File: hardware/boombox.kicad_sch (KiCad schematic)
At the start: 36 parts, among them J1 Micro_SD_Card_Det1, J4 USB_C_Receptacle_USB2.0_16P, SW1 SW_SPST, SW2 SW_SPST, SW3 SW_SPST, SW4 SW_SPST, SW5 SW_SPST, U1 Pico, U2 TMAG5231, U3 TMAG5231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

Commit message: Comitting so Nate can see errors
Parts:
- C11: value C_Small -> 0.1uF
- C3, C4: value C_Small -> 6pF
- J4: footprint (none) -> boombox:CUI_UJ20-C-H-C-4-SMT-TR
- U1: footprint RPi_Pico:RPi_Pico_SMD_TH -> boombox:RPi_Pico_SMD_TH
- U2, U3, U4, U5, U6: footprint (none) -> Package_TO_SOT_SMD:SOT-23
- Y1: footprint (none) -> boombox:XTAL_ECS-.327-6-13X
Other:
- title: (none) -> Boombuddy

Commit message: Routing
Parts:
- SW1: footprint boombox:PTS645S_SMTR92_CNK -> TestPoint:TestPoint_Pad_2.0x2.0mm
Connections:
- net BUTTONS0: now also SW1.1 (A); no longer SW1.2 (B)
- net BUTTONS1: now also SW2.1 (A); no longer SW2.2 (B)
- net BUTTONS2: now also SW3.1 (A); no longer SW3.2 (B)
- net BUTTONS3: now also SW4.1 (A); no longer SW4.2 (B)
- net BUTTONS4: now also SW5.1 (A); no longer SW5.2 (B)
- net SLP_PWR: now also SW1.2 (B), SW2.2 (B), SW3.2 (B), SW4.2 (B), SW5.2 (B); no longer SW1.1 (A), SW2.1 (A), SW3.1 (A), SW4.1 (A), SW5.1 (A)
- net USB_DN: now reaches J4.A7 (D-), J4.B7 (D-)
- net USB_DN: now also U1.45 (DP); no longer U1.44 (DN)
- net USB_DP: now reaches J4.A6 (D+), J4.B6 (D+)
- net USB_DP: now also U1.44 (DN); no longer U1.45 (DP)
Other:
- moved on the sheet: SW1, SW2, SW3, SW4, SW5
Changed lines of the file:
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@@
 	(wire
 		(pts
+			(xy 128.27 119.38) (xy 128.27 146.05)
+		)
+		(stroke
+			(width 0)
+			(type default)
+		)
+	)
+	(wire
+		(pts
 			(xy 92.71 158.75) (xy 92.71 146.05)
 		)
@@
 	(wire
 		(pts
+			(xy 107.95 111.76) (xy 107.95 146.05)
+		)
+		(stroke
+			(width 0)
+			(type default)
+		)
+	)
+	(wire
+		(pts
 			(xy 251.46 62.23) (xy 135.89 62.23)
 		)
@@
 	(wire
 		(pts
-			(xy 205.74 81.28) (xy 213.36 81.28)
+			(xy 97.79 109.22) (xy 97.79 146.05)
 		)
 		(stroke
@@
 	(wire
 		(pts
-			(xy 97.79 109.22) (xy 97.79 146.05)
+			(xy 205.74 81.28) (xy 213.36 81.28)
 		)
 		(stroke
@@
 	(wire
 		(pts
+			(xy 118.11 116.84) (xy 118.11 146.05)
+		)
+		(stroke
+			(width 0)
+			(type default)
+		)
+	)
+	(wire
+		(pts
 			(xy 77.47 96.52) (xy 138.43 96.52)
 		)
@@
 	(wire
 		(pts
-			(xy 118.11 146.05) (xy 118.11 116.84)
-		)
-		(stroke
-			(width 0)
-			(type default)
-		)
-	)
-	(wire
-		(pts
 			(xy 68.58 35.56) (xy 82.55 35.56)
 		)
@@
 	(wire
 		(pts
-			(xy 128.27 146.05) (xy 128.27 119.38)
-		)
-		(stroke
-			(width 0)
-			(type default)
-		)
-	)
-	(wire
-		(pts
 			(xy 48.26 72.39) (xy 93.98 72.39)
 		)
@@
 		)
 	)
-	(wire
-		(pts
-			(xy 107.95 146.05) (xy 107.95 111.76)
-		)
-		(stroke
-			(width 0)
-			(type default)
-		)
-	)
 	(bus
 		(pts
@@
 		)
 	)
+	(label "USB_DN"
+		(at 132.08 57.15 0)
+		(fields_autoplaced yes)
+		(effects
+			(font
+				(size 1.27 1.27)
+			)
+			(justify left bottom)
+		)
+	)
 	(label "BUTTONS2"
 		(at 102.87 158.75 90)
@@
 		)
 	)
+	(label "USB_DP"
+		(at 134.62 53.34 0)
+		(fields_autoplaced yes)
+		(effects
+			(font
+				(size 1.27 1.27)
+			)
+			(justify left bottom)
+		)
+	)
 	(symbol
 		(lib_id "Device:C_Small")
@@
 	(symbol
 		(lib_id "Switch:SW_SPST")
-		(at 92.71 138.43 270)
+		(at 92.71 138.43 90)
 		(unit 1)
 		(exclude_from_sim no)
@@
 		(dnp no)
 		(property "Reference" "SW2"
-			(at 89.916 136.398 0)
+			(at 95.504 140.462 0)
 			(effects
 				(font
@@
 		)
 		(property "Value" "SW_SPST"
-			(at 95.25 139.6999 90)
+			(at 90.17 137.1601 90)
 			(effects
 				(font
@@
 	(symbol
 		(lib_id "Switch:SW_SPST")
-		(at 123.19 138.43 270)
+		(at 123.19 138.43 90)
 		(unit 1)
 		(exclude_from_sim no)
@@
 		(dnp no)
 		(property "Reference" "SW5"
-			(at 120.904 136.398 0)
+			(at 125.476 140.462 0)
 			(effects
 				(font
@@
 		)
 		(property "Value" "SW_SPST"
-			(at 125.73 139.6999 90)
+			(at 120.65 137.1601 90)
 			(effects
 				(font
@@
 	(symbol
 		(lib_id "Switch:SW_SPST")
-		(at 113.03 138.43 270)
+		(at 113.03 138.43 90)
 		(unit 1)
 		(exclude_from_sim no)
@@
 		(dnp no)
 		(property "Reference" "SW4"
-			(at 110.744 136.398 0)
+			(at 115.316 140.462 0)
 			(effects
 				(font
@@
 		)
 		(property "Value" "SW_SPST"
-			(at 115.57 139.6999 90)
+			(at 110.49 137.1601 90)
 			(effects
 				(font
@@
 	(symbol
 		(lib_id "Switch:SW_SPST")
-		(at 102.87 138.43 270)
+		(at 102.87 138.43 90)
 		(unit 1)
 		(exclude_from_sim no)
@@
 		(dnp no)
 		(property "Reference" "SW3"
-			(at 100.33 136.398 0)
+			(at 105.41 140.462 0)
 			(effects
 				(font
@@
 		)
 		(property "Value" "SW_SPST"
-			(at 105.41 139.6999 90)
+			(at 100.33 137.1601 90)
 			(effects
 				(font
@@
 	(symbol
 		(lib_id "Switch:SW_SPST")
-		(at 81.28 138.43 270)
+		(at 81.28 138.43 90)
 		(unit 1)
 		(exclude_from_sim no)
@@
 		(dnp no)
 		(property "Reference" "SW1"
-			(at 77.978 135.89 0)
+			(at 84.582 140.97 0)
 			(effects
 				(font
@@
 		)
 		(property "Value" "SW_SPST"
-			(at 83.82 139.6999 90)
+			(at 78.74 137.1601 90)
 			(effects
 				(font
@@
 			)
 		)
-		(property "Footprint" "boombox:PTS645S_SMTR92_CNK"
+		(property "Footprint" "TestPoint:TestPoint_Pad_2.0x2.0mm"
 			(at 81.28 138.43 0)
 			(effects

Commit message: Switches
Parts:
- added TP1, TP10, TP2, TP3, TP4, TP5, TP6, TP7, TP8, TP9: ~, boombox:TestPoint_Pad_2.0x2.0mm, symbol Connector:TestPoint_Small
- added TP11, TP12: TestPoint_Small, boombox:TestPoint_Pad_2.0x2.0mm, symbol Connector:TestPoint_Small
- SW1: footprint TestPoint:TestPoint_Pad_2.0x2.0mm -> boombox:PTS645S_SMTR92_CNK
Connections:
- net BUTTONS0: now also TP2.1; no longer C5.1, SW1.1 (A), U1.15 (GPIO11)
- net BUTTONS1: now also TP4.1; no longer C6.1, SW2.1 (A), U1.16 (GPIO12)
- net BUTTONS2: now also TP6.1; no longer C7.1, SW3.1 (A), U1.17 (GPIO13)
- net BUTTONS3: now also TP8.1; no longer C8.1, SW4.1 (A), U1.19 (GPIO14)
- net BUTTONS4: now also TP10.1; no longer C9.1, SW5.1 (A), U1.20 (GPIO15)
- net SLP_PWR: now also TP11.1; no longer SW1.2 (B), SW2.2 (B), SW3.2 (B), SW4.2 (B), SW5.2 (B)
- new net: C8.1, SW4.1 (A), TP7.1, U1.19 (GPIO14)
- new net: C5.1, SW1.1 (A), TP1.1, U1.15 (GPIO11)
- new net: C7.1, SW3.1 (A), TP5.1, U1.17 (GPIO13)
- new net: C6.1, SW2.1 (A), TP3.1, U1.16 (GPIO12)
- new net: C9.1, SW5.1 (A), TP9.1, U1.20 (GPIO15)
- new net BTN_PWR: SW1.2 (B), SW2.2 (B), SW3.2 (B), SW4.2 (B), SW5.2 (B), TP12.1
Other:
- moved on the sheet: C5, C6, C7, C8, C9

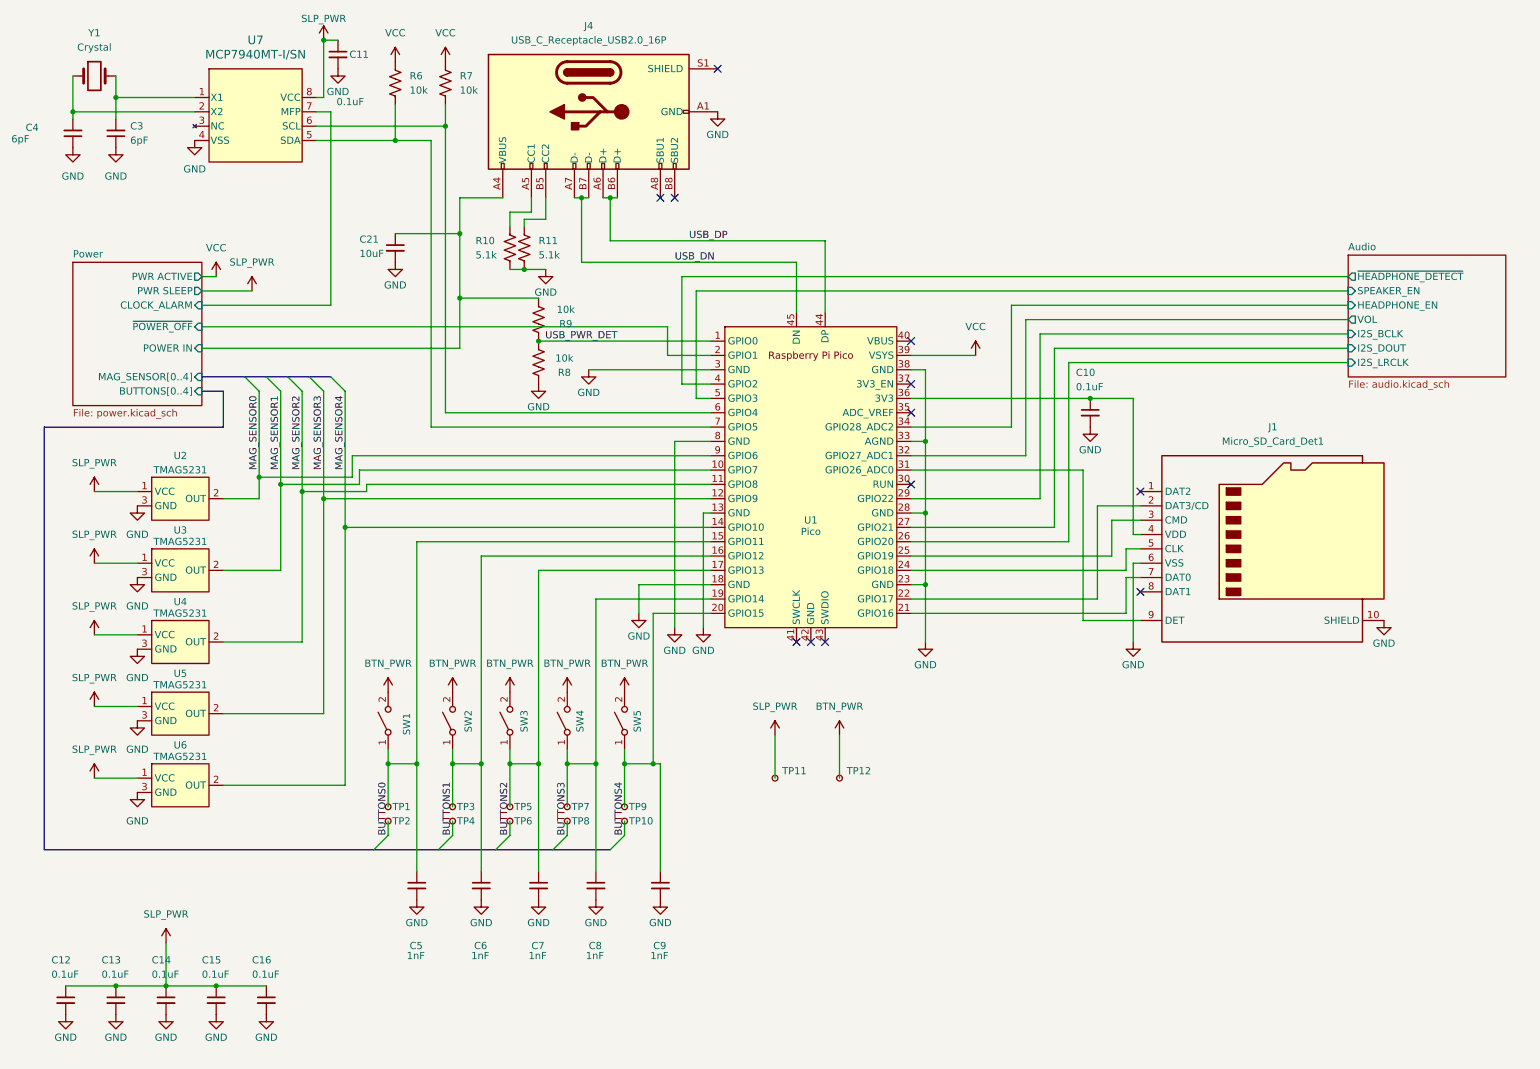
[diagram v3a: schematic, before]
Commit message: Resized cartridge and moved around things
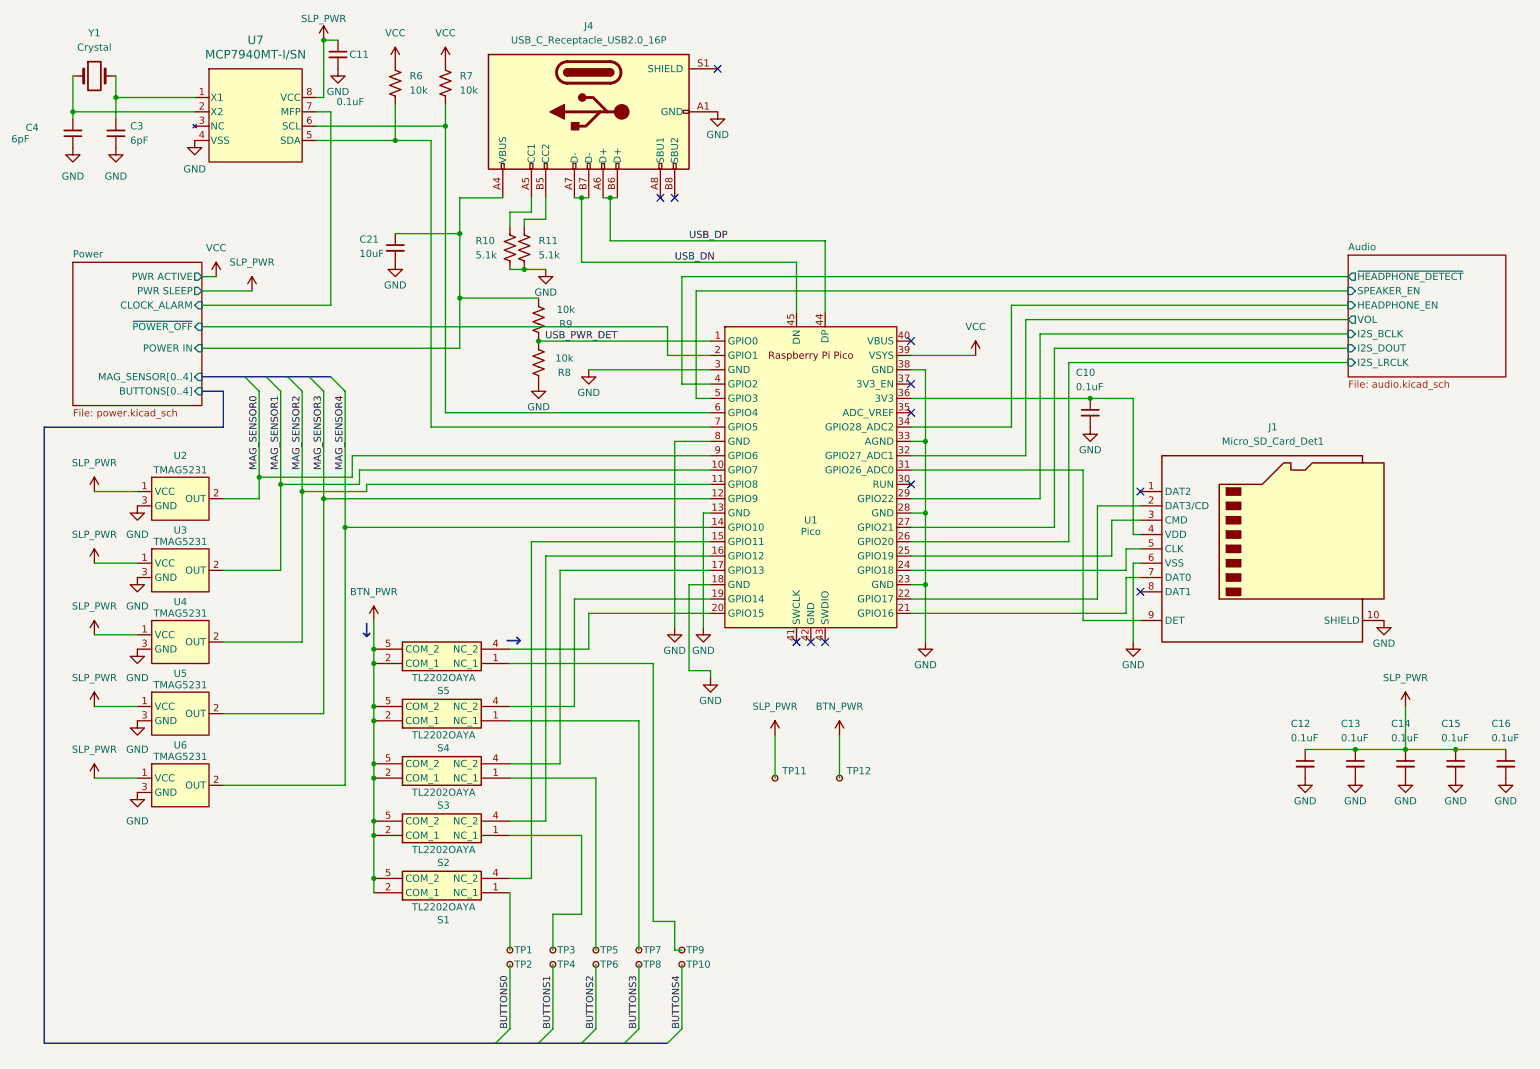
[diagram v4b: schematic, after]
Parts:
- removed C5, C6, C7, C8, C9: 1nF, Capacitor_SMD:C_0402_1005Metric_Pad0.74x0.62mm_HandSolder, symbol Device:C_Small
- removed SW1, SW2, SW3, SW4, SW5: SW_SPST, boombox:PTS645S_SMTR92_CNK, symbol Switch:SW_SPST
- added S1, S2, S3, S4, S5: TL2202OAYA, TL2202OAYA, symbol boombox:TL2202OAYA
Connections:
- net BTN_PWR: now also S1.2 (COM_1), S1.5 (COM_2), S2.2 (COM_1), S2.5 (COM_2), S3.2 (COM_1), S3.5 (COM_2), S4.2 (COM_1), S4.5 (COM_2), S5.2 (COM_1), S5.5 (COM_2)
- net at TP7.1: now also S4.1 (NC_1); no longer U1.19 (GPIO14)
- net at TP1.1: now also S1.1 (NC_1); no longer U1.15 (GPIO11)
- net at U1.17 (GPIO13): now also S3.4 (NC_2); no longer TP5.1
- net at TP3.1: now also S2.1 (NC_1); no longer U1.16 (GPIO12)
- net at U1.20 (GPIO15): now also S5.4 (NC_2); no longer TP9.1
- new net: S1.4 (NC_2), U1.15 (GPIO11)
- new net: S2.4 (NC_2), U1.16 (GPIO12)
- new net: S4.4 (NC_2), U1.19 (GPIO14)
- new net: S5.1 (NC_1), TP9.1
- new net: S3.1 (NC_1), TP5.1
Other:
- note added: "↓"
- moved on the sheet: C12, C13, C14, C15, C16, TP1, TP10, TP2, TP3, TP4, TP5, TP6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

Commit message: Almost done TM
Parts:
- removed TP10, TP6, TP7, TP9: ~, boombox:TestPoint_Pad_2.0x2.0mm, symbol Connector:TestPoint_Small
- removed TP11: TestPoint_Small, boombox:TestPoint_Pad_2.0x2.0mm, symbol Connector:TestPoint_Small
- added J2: Screw_Terminal_01x07, boombox:1990054, symbol Connector:Screw_Terminal_01x07
- TP1, TP2, TP3, TP4, TP5, TP8: value ~ -> TestPoint_Small
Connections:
- net BUTTONS1 is gone; now on an unnamed net: TP4.1
- net BUTTONS3 is gone; now on an unnamed net: TP8.1
- net SLP_PWR: now also J2.2 (Pin_2)
- net at S4.1 (NC_1): now also S1.1 (NC_1), S2.1 (NC_1), S3.1 (NC_1), S5.1 (NC_1)
- net at TP3.1: now also S3.4 (NC_2); no longer S2.1 (NC_1)
- net at TP1.1: now also S1.4 (NC_2); no longer S1.1 (NC_1)
- net at U1.15 (GPIO11): now also J2.7 (Pin_7); no longer S1.4 (NC_2)
- net at U1.16 (GPIO12): now also J2.6 (Pin_6); no longer S2.4 (NC_2)
- net at U1.17 (GPIO13): now also J2.5 (Pin_5); no longer S3.4 (NC_2)
- net at S4.4 (NC_2): no longer U1.19 (GPIO14)
- net at S5.4 (NC_2): now also TP5.1; no longer U1.20 (GPIO15)
- net BUTTONS0: no longer names the net of TP2.1
- net BUTTONS0: now also S2.4 (NC_2)
- new net: J2.4 (Pin_4), U1.19 (GPIO14)
- new net: J2.3 (Pin_3), U1.20 (GPIO15)
- new net Power/BTN_LATCH: J2.1 (Pin_1)
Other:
- sheet Power ports: added BTN_LATCH; removed BUTTONS[0..4]
- moved on the sheet: TP12

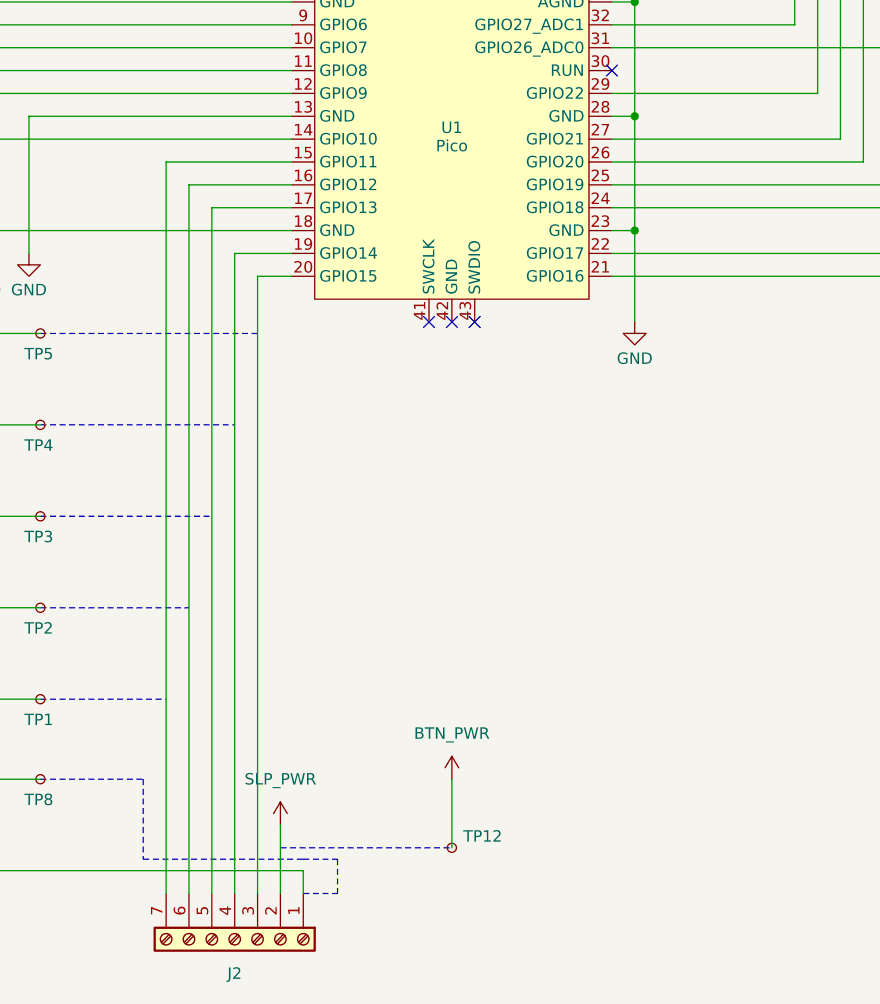
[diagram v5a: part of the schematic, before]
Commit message: Added debouncing caps
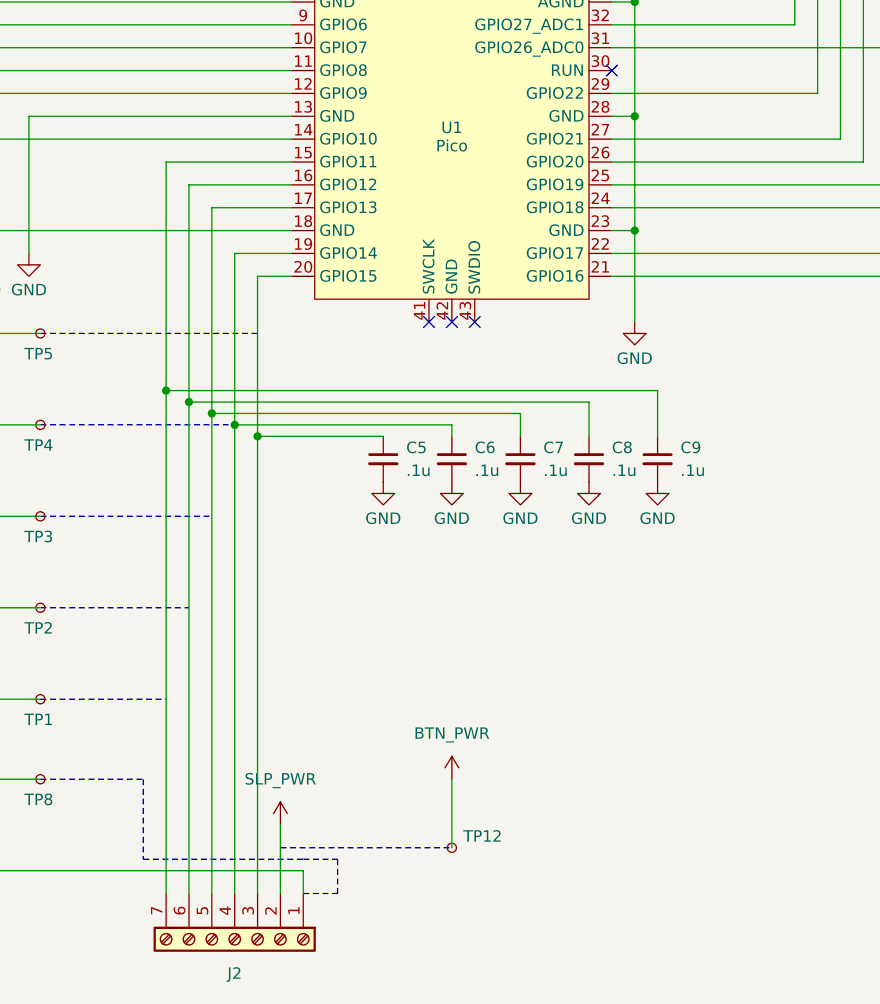
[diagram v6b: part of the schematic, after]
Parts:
- added C5, C6, C7, C8, C9: .1u, Capacitor_SMD:C_0402_1005Metric_Pad0.74x0.62mm_HandSolder, symbol Device:C_Small
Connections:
- net GND: now also C5.2, C6.2, C7.2, C8.2, C9.2
- net at J2.7 (Pin_7), U1.15 (GPIO11): now also C9.1
- net at J2.6 (Pin_6), U1.16 (GPIO12): now also C8.1
- net at J2.5 (Pin_5), U1.17 (GPIO13): now also C7.1
- net at J2.4 (Pin_4), U1.19 (GPIO14): now also C6.1
- net at J2.3 (Pin_3), U1.20 (GPIO15): now also C5.1

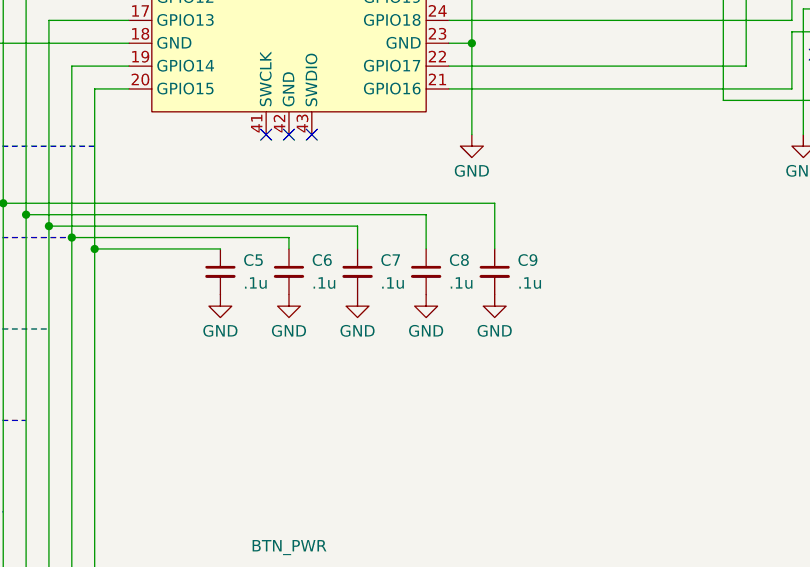
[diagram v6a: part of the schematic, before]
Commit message: Reading from SD card
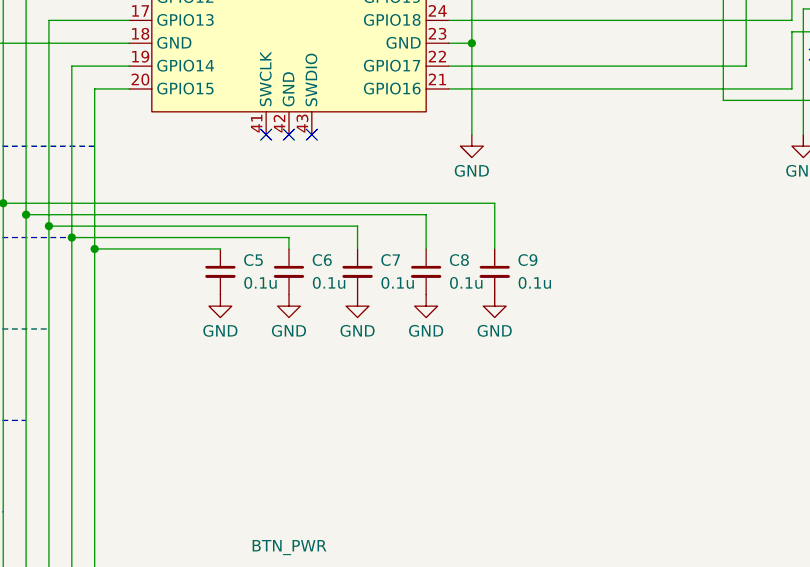
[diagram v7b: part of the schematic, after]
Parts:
- C5, C6, C7, C8, C9: value .1u -> 0.1u
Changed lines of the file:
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@@
 			)
 		)
-		(property "Value" ".1u"
+		(property "Value" "0.1u"
 			(at 181.61 140.9762 0)
 			(effects
@@
 			)
 		)
-		(property "Value" ".1u"
+		(property "Value" "0.1u"
 			(at 166.37 140.9762 0)
 			(effects
@@
 			)
 		)
-		(property "Value" ".1u"
+		(property "Value" "0.1u"
 			(at 158.75 140.9762 0)
 			(effects
@@
 			)
 		)
-		(property "Value" ".1u"
+		(property "Value" "0.1u"
 			(at 151.13 140.9762 0)
 			(effects
@@
 			)
 		)
-		(property "Value" ".1u"
+		(property "Value" "0.1u"
 			(at 173.99 140.9762 0)
 			(effects
